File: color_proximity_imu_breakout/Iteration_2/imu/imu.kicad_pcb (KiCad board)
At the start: 2 copper layers, 12.6 x 16.5 mm, 11 parts, among them J4 Conn_01x05, U6 ICM-20602

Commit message: imu updated iteration 2
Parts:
- removed the G*** at (124.4, 134.3)
- removed J4 (x2): Conn_01x05, Connector_PinHeader_2.54mm:PinHeader_1x05_P2.54mm_Vertical
- added ?: , , F.Cu at (142.4, 128.3)
- added ?: , , F.Cu at (148.8, 141.0)
- added C1: 10u, Capacitor_SMD:C_0603_1608Metric_Pad1.08x0.95mm_HandSolder, F.Cu at (149.0, 133.4)
- added C2: 10u, Capacitor_SMD:C_0603_1608Metric_Pad1.08x0.95mm_HandSolder, F.Cu at (150.8, 133.5)
- added G***: LOGO, pcb_footprints:vexu_ghost, B.Cu at (141.8, 138.2)
- added G***: LOGO, pcb_footprints:ras, B.Cu at (144.2, 142.2)
- added J1: Conn_01x10, pcb_footprints:GT-B0502MSV27-10S1101, F.Cu at (148.8, 128.3)
- added J2: Conn_01x10, pcb_footprints:GT-B0502MSV27-10S1101, F.Cu at (142.4, 141.0)
- moved C13 28.0 mm to (149.0, 137.0), turned to 90 degrees
- moved R19 22.6 mm to (146.8, 132.2)
- moved C8 21.9 mm to (150.8, 137.1), turned to 90 degrees
- moved C10 20.2 mm to (147.4, 135.0), turned to -90 degrees
- moved U6 18.6 mm to (145.0, 135.4), turned to 0 degrees
- moved C7 17.6 mm to (145.4, 132.2)
- moved G*** 16.1 mm to (146.6, 136.8)
- moved C9 14.4 mm to (144.0, 132.2), turned to 90 degrees
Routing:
- net +5V: track 0.02 -> 20.6 mm
- net /sda: track 16.3 -> 29.4 mm, vias 1 -> 3
- net Net-(U6-~{CS}): track 1.34 -> 11.4 mm, vias 0 -> 2
- net +3.3V: track 33.0 -> 37.3 mm, vias 2 -> 0
- net GND: track 6.80 -> 10.3 mm, vias 4 -> 7
- net /scl: track 17.3 -> 19.8 mm, vias 1 -> 3
- net Net-(U6-REGOUT): track 2.10 -> 2.62 mm
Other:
- board size 12.6 x 16.5 mm -> 13 x 20 mm
- board text added: "Designed By Gengwen Li Trung Le"
- board text removed: "3V3"
- board text removed: "5V"
- board text removed: "Designed By Gengwen Li"
- board text removed: "GND"
- board text removed: "SCL"
- board text removed: "SDA"

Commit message: imu board iteration 2 updated
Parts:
- removed C13: 10u, Capacitor_SMD:C_0603_1608Metric_Pad1.08x0.95mm_HandSolder
- moved C2 3.97 mm to (149.0, 137.0), turned to -90 degrees
- moved C1 1.52 mm to (150.4, 132.8)
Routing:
- net GND: track 10.3 -> 11.1 mm

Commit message: breakout board iteration 2 updates
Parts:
- moved C2 1.00 mm to (149.0, 136.0)
- moved C8 0.64 mm to (150.8, 136.5)
- moved C7 0.17 mm to (145.4, 132.0)
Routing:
- net GND: track 11.1 -> 13.1 mm
- net /sda: track 29.4 -> 28.6 mm

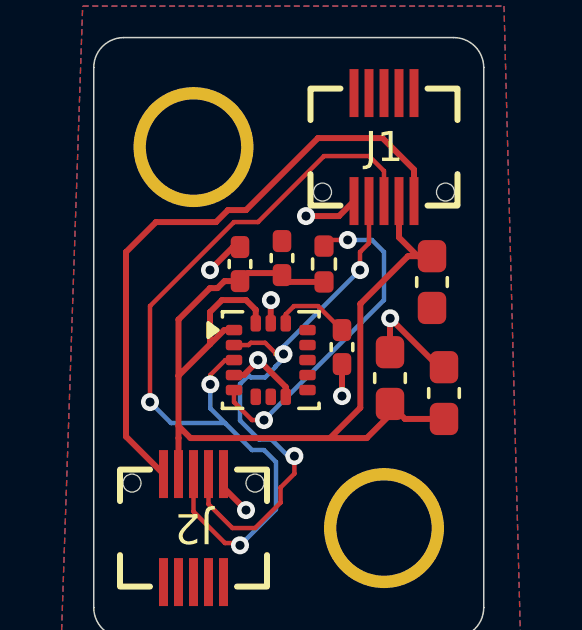
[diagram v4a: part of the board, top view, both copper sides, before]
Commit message: updated host schematic and imu production files
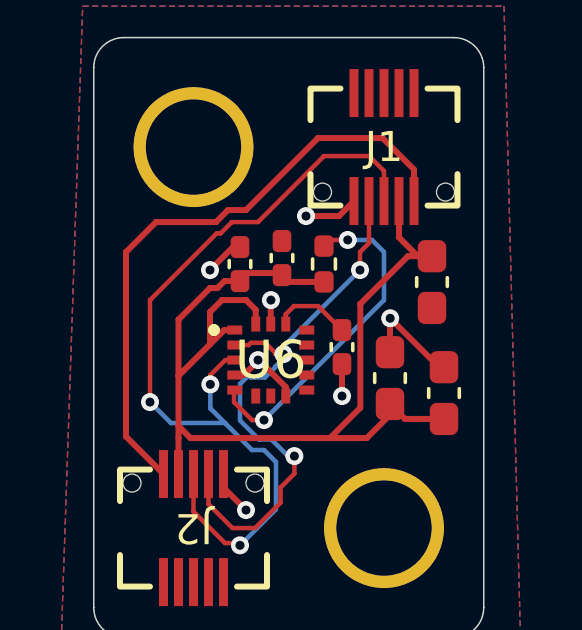
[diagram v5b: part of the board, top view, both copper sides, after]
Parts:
- U6: footprint Package_LGA:LGA-16_3x3mm_P0.5mm_LayoutBorder3x5y -> pcb_footprints:IAM20680HP

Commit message: updated production files
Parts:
- removed the G*** at (146.6, 136.8)
- removed the G*** at (144.2, 142.2)
- G***: moved to F.Cu
- J1, J2: moved to B.Cu
- moved G*** 12.9 mm to (148.9, 127.4), turned to 0 degrees
- turned C1 to -90 degrees
- turned C2 to 90 degrees
- turned J1 to 180 degrees
- turned J2 to 0 degrees
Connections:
- C1 pad 1: GND -> +3.3V
- C1 pad 2: +3.3V -> GND
- C2 pad 1: GND -> +3.3V
- C2 pad 2: +3.3V -> GND
- J1 pad 10: +5V -> GND
- J1 pad 6: GND -> unconnected-(J1-Pin_6-Pad6)
- J1 pad 7: /scl -> +3.3V
- J1 pad 9: +3.3V -> /scl
- J2 pad 10: +5V -> GND
- J2 pad 6: GND -> unconnected-(J2-Pin_6-Pad6)
- J2 pad 7: /scl -> +3.3V
- J2 pad 9: +3.3V -> /scl
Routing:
- net +5V: track 20.6 -> 0.00 mm
- net /sda: track 28.8 -> 17.0 mm, vias 3 -> 1
- net /scl: track 19.5 -> 13.2 mm, vias 3 -> 1
- net GND: track 13.1 -> 10.00 mm, vias 7 -> 6
- net +3.3V: track 36.7 -> 37.2 mm, vias 0 -> 2
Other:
- board text added: "Designed By: Gengwen Li Trung Le"
- board text removed: "Designed By Gengwen Li Trung Le"
